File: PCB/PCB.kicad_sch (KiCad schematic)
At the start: 20 parts, among them SW1 SW4_Push, SW10 SW2_Push, SW11 SW3_Push, SW2 SW5_Push, SW3 RotaryEncoder_Switch, SW4 RotaryEncoder_Switch, SW5 SW6_Push, SW6 SW7_Push, SW7 SW_Push-Mode0, SW8 SW_Push-Mode1, SW9 SW1_Push, U4 ER_OLEDM0.91_1x-I2C, U5 MOUDLE-SEEEDUINO-XIAO

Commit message: Add Hakin Pad bill of materials
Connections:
- net at SW11.2, U5.3 (PA10_A2_D2): now also SW10.2, SW9.2; no longer SW5.2
- net at SW1.2, U5.4 (PA11_A3_D3): now also SW2.2, SW5.2; no longer SW6.2
- net at U5.10 (PA5_A9_D9_MISO): now also SW3.B; no longer SW4.S1
- net at U5.11 (PA6_A10_D10_MOSI): no longer SW4.A
- net at U5.12 (3V3): now also U4.2 (VCC); no longer SW3.S1
- net at U5.14 (5V): no longer U4.2 (VCC)
- net at U5.8 (PB09_A7_D7_RX): now also D3.1 (K), D6.1 (K); no longer SW3.B
- net at D5.1 (K): now also D2.1 (K), U5.2 (PA4_A1_D1); no longer D4.1 (K)
- new net: SW6.2, U5.7 (PB08_A6_D6_TX)
- new net: D1.1 (K), D4.1 (K), D7.1 (K), U5.1 (PA02_A0_D0)
- new net: SW3.C, SW3.S1, SW7.2, SW8.2, U4.1 (GND), U5.13 (GND)
- new net: U4.4 (SDA), U5.5 (PA8_A4_D4_SDA)
- new net: U4.3 (SCL), U5.6 (PA9_A5_D5_SCL)
- new net: SW3.A, U5.9 (PA7_A8_D8_SCK)
- now unconnected: SW3.S2, SW4.B, SW4.C, SW4.S2, SW7.1, SW8.1
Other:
- moved on the sheet: D1, D2, D3, D4, D5, D6, D7

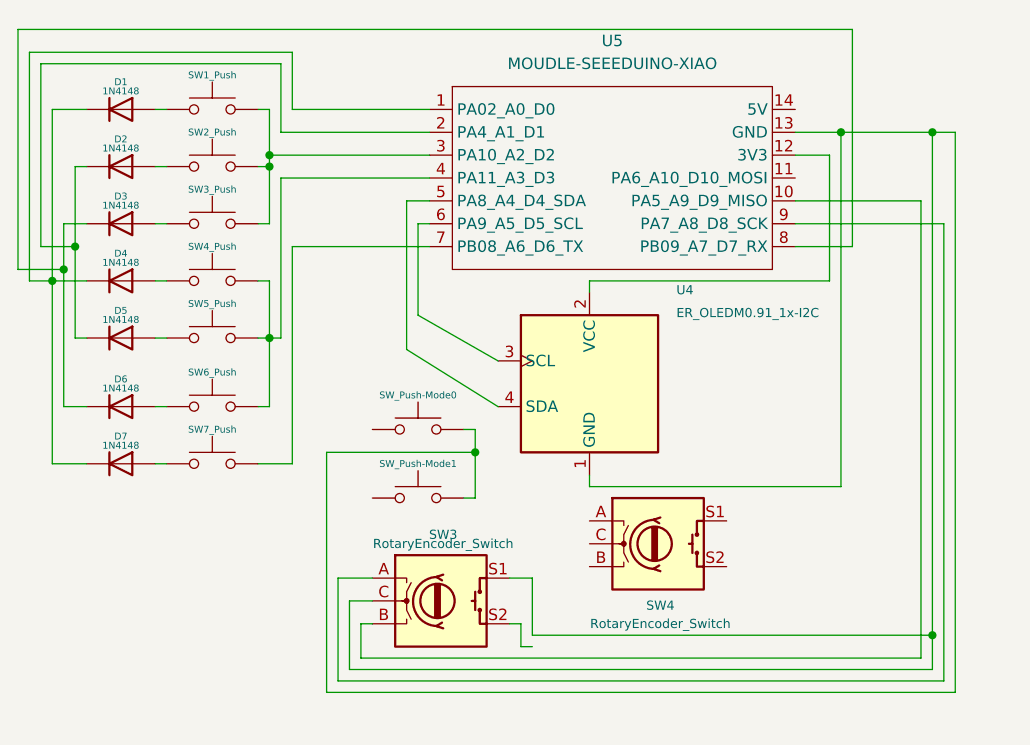
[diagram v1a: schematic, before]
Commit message: Restore original Hakin Pad schematic
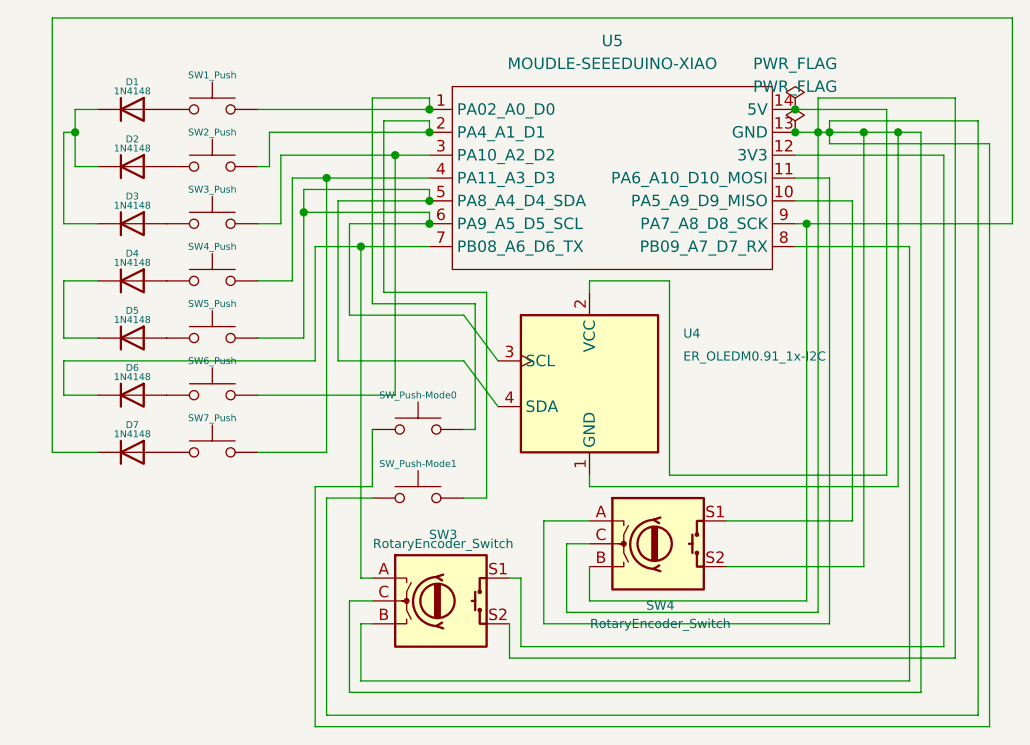
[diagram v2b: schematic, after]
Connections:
- net at SW11.2, U5.3 (PA10_A2_D2): now also SW5.2; no longer SW10.2, SW9.2
- net at SW6.2: now also SW1.2, U5.4 (PA11_A3_D3); no longer U5.7 (PB08_A6_D6_TX)
- net at U5.10 (PA5_A9_D9_MISO): now also SW4.S1; no longer SW3.B
- net at U5.11 (PA6_A10_D10_MOSI): now also SW4.A
- net at U5.12 (3V3): now also SW3.S1; no longer U4.2 (VCC)
- net at SW3.C, U4.1 (GND), U5.13 (GND): now also SW3.S2, SW4.C, SW4.S2, SW7.1, SW8.1; no longer SW3.S1, SW7.2, SW8.2
- net at U5.14 (5V): now also U4.2 (VCC)
- net at U4.4 (SDA), U5.5 (PA8_A4_D4_SDA): now also SW2.2, U4.3 (SCL), U5.6 (PA9_A5_D5_SCL)
- net at U5.9 (PA7_A8_D8_SCK): now also D7.1 (K), SW4.B; no longer SW3.A
- new net: D1.1 (K), D2.1 (K), D3.1 (K)
- new net: SW7.2, SW9.2, U5.1 (PA02_A0_D0)
- new net: SW10.2, SW8.2, U5.2 (PA4_A1_D1)
- new net: D6.1 (K), SW3.A, U5.7 (PB08_A6_D6_TX)
- new net: SW3.B, U5.8 (PB09_A7_D7_RX)
- new net: D4.1 (K), D5.1 (K)
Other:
- moved on the sheet: D1, D2, D3, D4, D5, D6, D7
